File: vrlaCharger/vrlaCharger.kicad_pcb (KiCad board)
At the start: 2 copper layers, 43 x 27 mm, 20 parts, among them J1 Conn_01x02, J2 Conn_01x02, Q1 Q_PMOS_GSD, Q2 Q_NPN_BEC, U1 LM317_3PinPackage

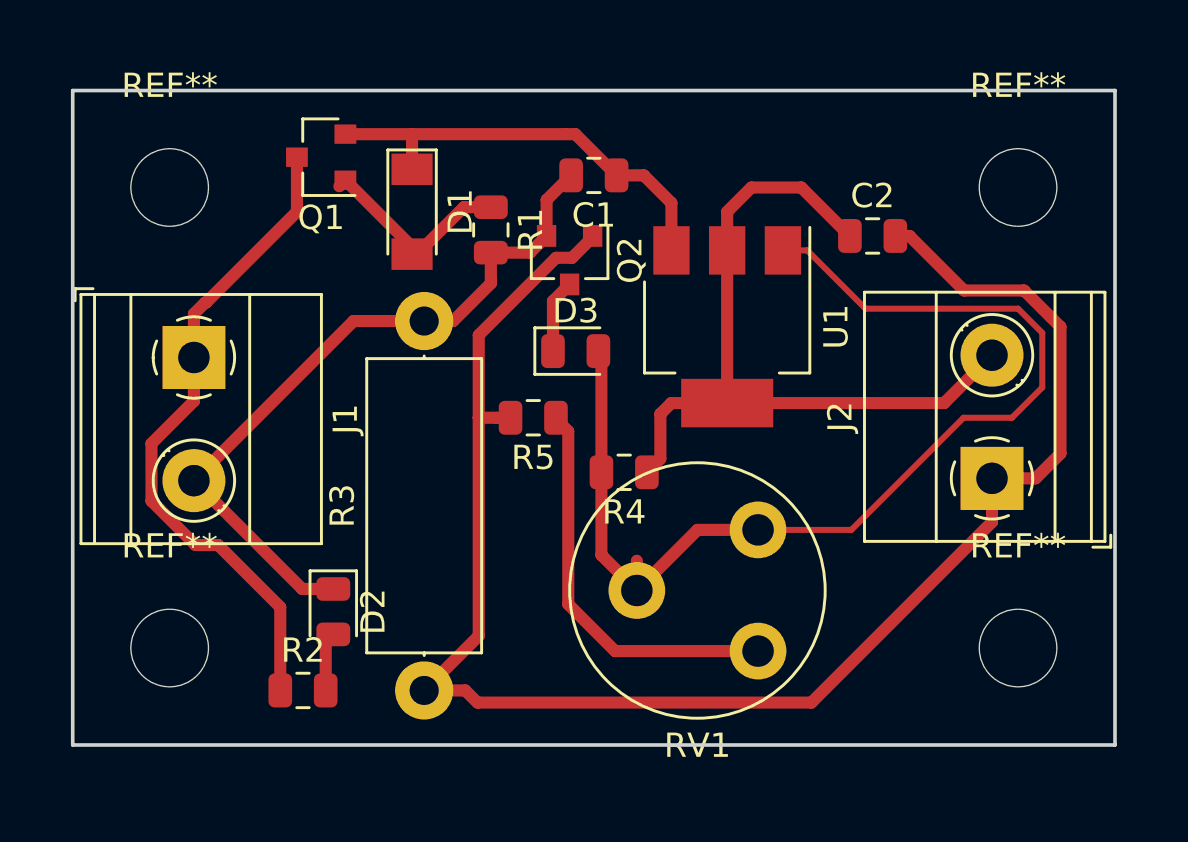
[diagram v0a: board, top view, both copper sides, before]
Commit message: THT elements flipped to other side
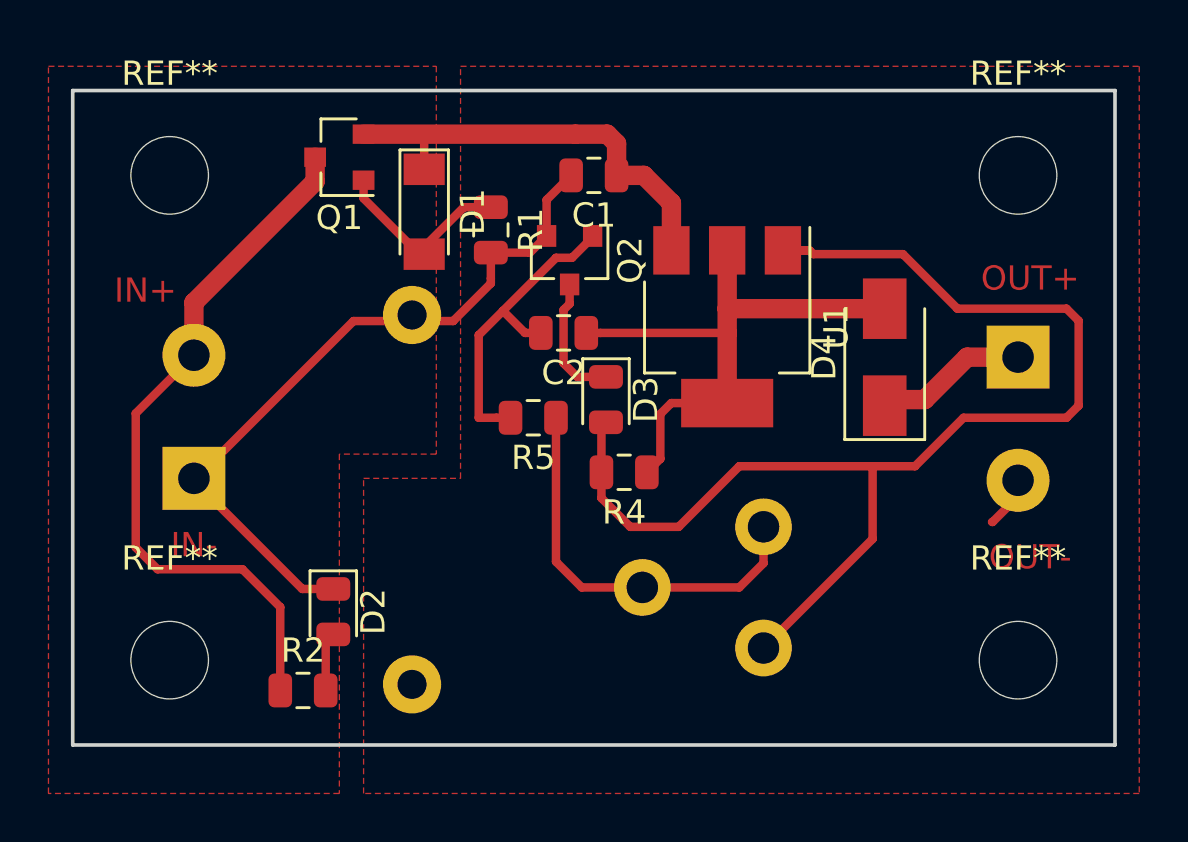
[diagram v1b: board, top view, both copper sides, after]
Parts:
- added D4: D_Schottky, Diode_SMD:D_SMA, F.Cu at (88.5, 123.0)
- J1, J2, R3, RV1: moved to B.Cu
- moved C2 13.4 mm to (75.2, 122.0), turned to 180 degrees
- moved J2 5.11 mm to (94.0, 123.0), turned to 270 degrees
- moved J1 4.99 mm to (60.0, 128.0), turned to 90 degrees
- moved RV1 4.88 mm to (83.5, 135.0)
- moved D3 2.36 mm to (77.0, 124.8), turned to 270 degrees
- moved Q1 0.75 mm to (66.0, 114.8)
- moved R3 0.56 mm to (69.0, 136.5)
- moved D1 0.50 mm to (69.5, 117.0)
- moved REF** 0.50 mm to (94.0, 135.5)
- moved REF** 0.50 mm to (94.0, 115.5)
- moved REF** 0.50 mm to (59.0, 115.5)
- moved REF** 0.50 mm to (59.0, 135.5)
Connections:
- J1 pad 1: Net-(J1-Pad1) -> Net-(C1-Pad2)
- J1 pad 2: Net-(C1-Pad2) -> Net-(J1-Pad2)
- J2 pad 1: Net-(C2-Pad2) -> Net-(D4-Pad1)
- J2 pad 2: Net-(C2-Pad1) -> Net-(C2-Pad2)
- Q1 pad 3: Net-(J1-Pad1) -> Net-(J1-Pad2)
- R2 pad 1: Net-(J1-Pad1) -> Net-(J1-Pad2)
- RV1 pad 2: Net-(D3-Pad2) -> Net-(R5-Pad1)
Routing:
- net Net-(C2-Pad2): track 68.7 -> 15.3 mm
- net Net-(J1-Pad2): track 0.00 -> 29.7 mm
- net Net-(J1-Pad1): track 27.3 -> 0.00 mm
- net Net-(C2-Pad1): track 31.5 -> 24.2 mm
- net Net-(D3-Pad2): track 46.3 -> 52.7 mm
- net Net-(D4-Pad1): track 0.00 -> 6.33 mm
- net Net-(D3-Pad1): track 3.03 -> 5.34 mm
- added copper zone on F.Cu, net Net-(C1-Pad2)
- added copper zone on F.Cu, net Net-(C2-Pad2)
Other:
- net class Default: trace_width 0.25 -> 0.35
- board text added: "IN+"
- board text added: "IN-"
- board text added: "OUT+"
- board text added: "OUT-"
